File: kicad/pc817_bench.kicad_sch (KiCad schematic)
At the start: 15 parts, among them J1 24V + e-stops, U1 PC817, U2 PC817

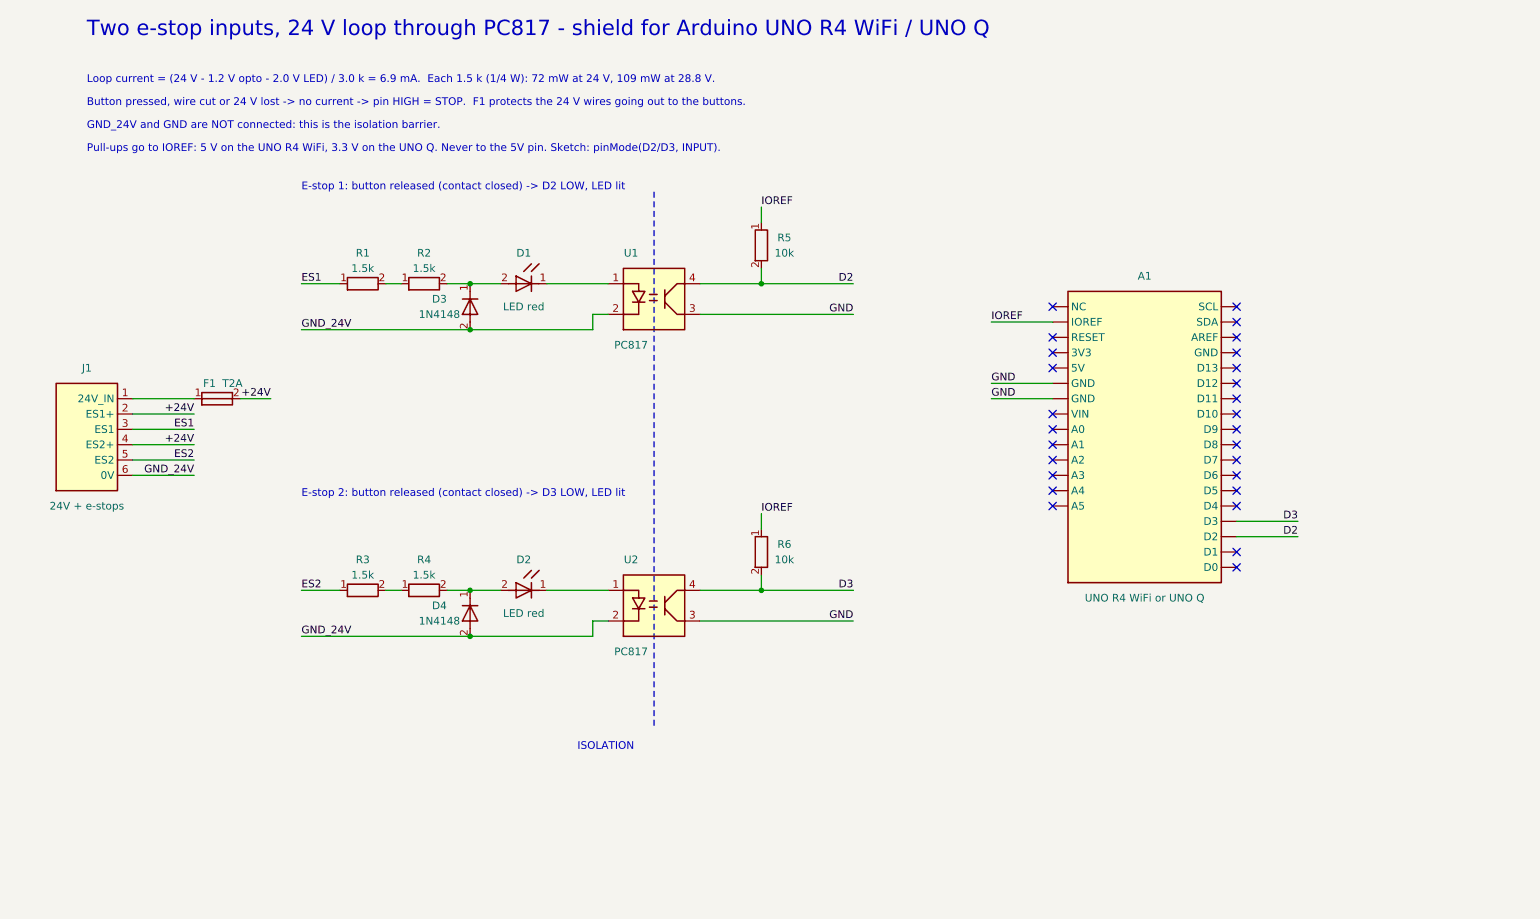
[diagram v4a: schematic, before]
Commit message: Four channels: two e-stop loops (D2, D3) and two lidar inputs (D4, D5)
9-way 3.5 mm terminal, fuse on the 24 V going out to the buttons, channels at
10 mm pitch. DRC: no errors, schematic parity OK (KiCad 10.0.6).

Co-Authored-By: Claude Fable 5.1 <noreply@anthropic.com>
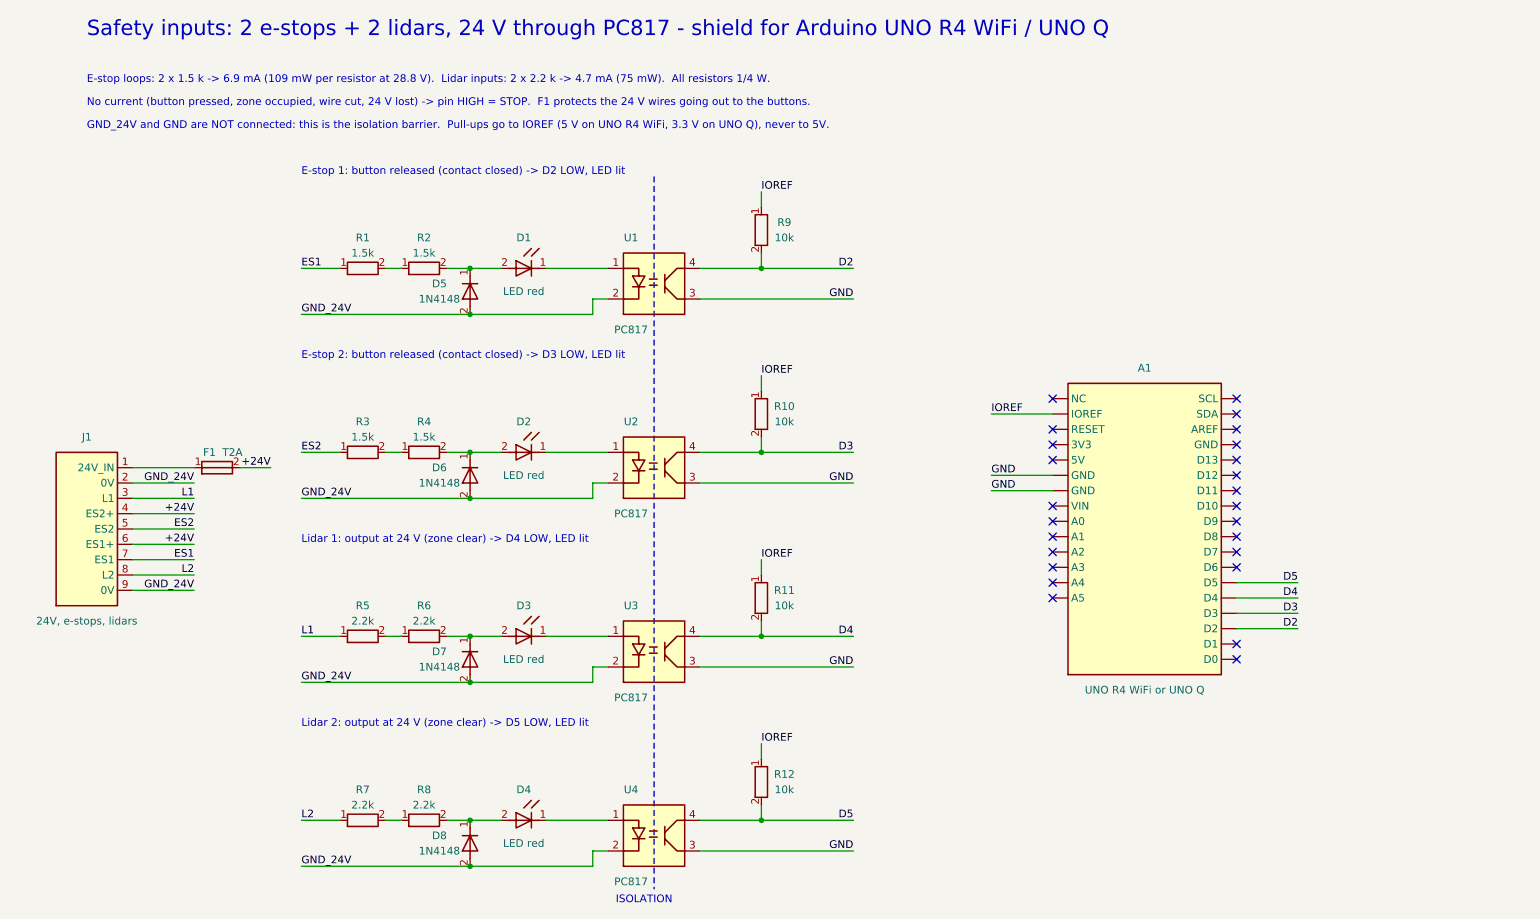
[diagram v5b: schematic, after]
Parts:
- removed J1: 24V + e-stops, TerminalBlock_Phoenix:TerminalBlock_Phoenix_MKDS-1,5-6_1x06_P5.00mm_Horizontal, symbol bench:CONN6
- added D4: LED red, LED_THT:LED_D3.0mm, symbol bench:LED_H
- added D7, D8: 1N4148, Diode_THT:D_DO-35_SOD27_P7.62mm_Horizontal, symbol bench:D_V
- added F1: T2A, Fuse:Fuse_Littelfuse_372_D8.50mm, symbol bench:FUSE_H
- added J1: 24V, e-stops, lidars, TerminalBlock_Phoenix:TerminalBlock_Phoenix_PT-1,5-9-3.5-H_1x09_P3.50mm_Horizontal, symbol bench:CONN9
- added R11, R12: 10k, Resistor_THT:R_Axial_DIN0207_L6.3mm_D2.5mm_P10.16mm_Horizontal, symbol bench:R_V
- added R5, R6, R7, R8: 2.2k, Resistor_THT:R_Axial_DIN0207_L6.3mm_D2.5mm_P10.16mm_Horizontal, symbol bench:R_H
- added U3, U4: PC817, Package_DIP:DIP-4_W7.62mm, symbol bench:PC817
- D3: renamed from F1; value T2A -> LED red; footprint Fuse:Fuse_Littelfuse_372_D8.50mm -> LED_THT:LED_D3.0mm; symbol bench:FUSE_H -> bench:LED_H
- renumbered D3 to D5, D4 to D6, R6 to R10, R5 to R9
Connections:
- net +24V: now also F1.2, J1.4 (ES2+), J1.6 (ES1+); no longer D3.2
- net ES1: now also J1.7 (ES1)
- net ES2: now also J1.5 (ES2)
- net GND: now also U3.3 (E), U4.3 (E)
- net GND_24V: now also D7.2 (A), D8.2 (A), J1.2 (0V), J1.9 (0V), U3.2 (K), U4.2 (K)
- net IOREF: now also R11.1, R12.1
- net at D3.1 (K): now also U3.1 (A)
- net D4: now reaches A1.19 (D4)
- net D4: now also R11.2, U3.4 (C)
- net D5: now reaches A1.20 (D5)
- net D5: now also R12.2, U4.4 (C)
- new net: D4.1 (K), U4.1 (A)
- new net: D3.2 (A), D7.1 (K), R6.2
- new net: R5.2, R6.1
- new net: R7.2, R8.1
- new net: D4.2 (A), D8.1 (K), R8.2
- new net: F1.1, J1.1 (24V_IN)
- new net L1: J1.3 (L1), R5.1
- new net L2: J1.8 (L2), R7.1
- no-connect marks 27 -> 25
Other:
- note added: "E-stop loops: 2 x 1.5 k -> 6.9 mA (109 mW per resistor at 28.8 V). Lidar inputs: 2 x 2.2 k -> 4.7 mA (75 mW). All resistors 1/4 W."
- note added: "GND_24V and GND are NOT connected: this is the isolation barrier. Pull-ups go to IOREF (5 V on UNO R4 WiFi, 3.3 V on UNO Q), never to 5V."
- note added: "Lidar 1: output at 24 V (zone clear) -> D4 LOW, LED lit"
- note added: "Lidar 2: output at 24 V (zone clear) -> D5 LOW, LED lit"
- note added: "No current (button pressed, zone occupied, wire cut, 24 V lost) -> pin HIGH = STOP. F1 protects the 24 V wires going out to the buttons."
- note added: "Safety inputs: 2 e-stops + 2 lidars, 24 V through PC817 - shield for Arduino UNO R4 WiFi / UNO Q"
- note removed: "Button pressed, wire cut or 24 V lost -> no current -> pin HIGH = STOP. F1 protects the 24 V wires going out to the buttons."
- note removed: "GND_24V and GND are NOT connected: this is the isolation barrier."
- note removed: "Loop current = (24 V - 1.2 V opto - 2.0 V LED) / 3.0 k = 6.9 mA. Each 1.5 k (1/4 W): 72 mW at 24 V, 109 mW at 28.8 V."
- note removed: "Pull-ups go to IOREF: 5 V on the UNO R4 WiFi, 3.3 V on the UNO Q. Never to the 5V pin. Sketch: pinMode(D2/D3, INPUT)."
- note removed: "Two e-stop inputs, 24 V loop through PC817 - shield for Arduino UNO R4 WiFi / UNO Q"
- title: E-stop inputs: 24 V loop through PC817 -> Safety inputs: 2 e-stops + 2 lidars
- moved on the sheet: D1, D2, D5, D6, R1, R10, R2, R3, R4, R9, U1, U2

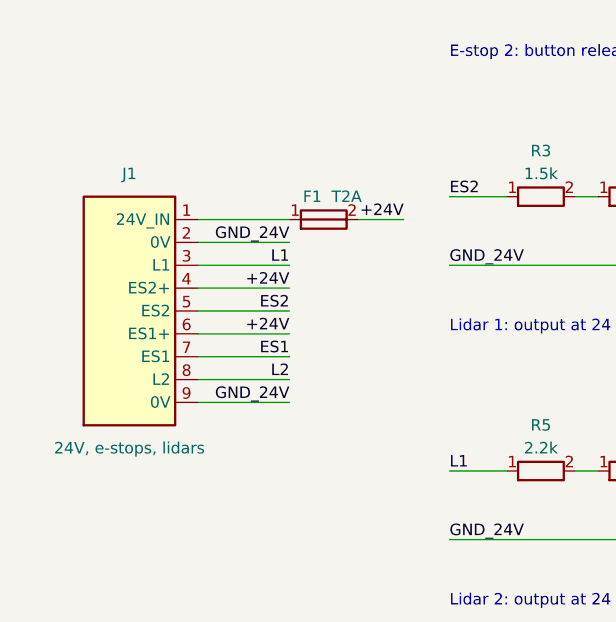
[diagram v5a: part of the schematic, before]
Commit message: Proto-shield variant in KiCad: grid footprints, 8-way terminal, board file models the build plan
Solder bridges and bare-wire runs are solder-side tracks; insulated wires stay
as ratsnest. check.sh verifies parity with the schematic and the wire count.
Plan reworked for physical clearances (diode away from the LED, fuse clear of
the header and terminal): 16 x 16 pads.

Co-Authored-By: Claude Fable 5.1 <noreply@anthropic.com>
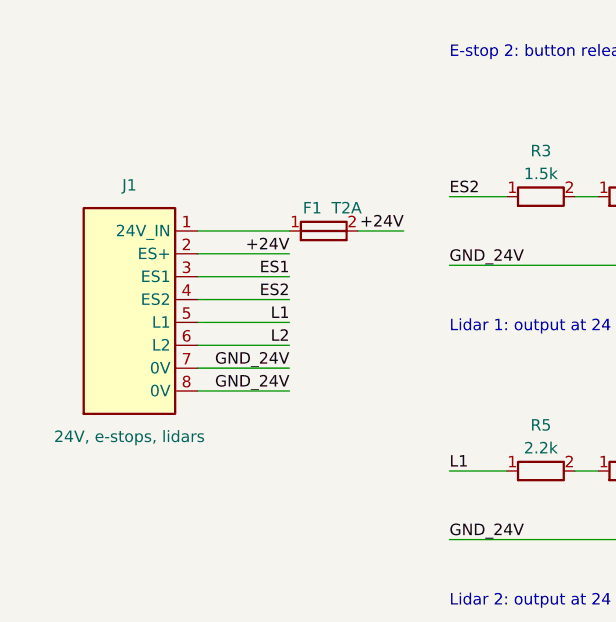
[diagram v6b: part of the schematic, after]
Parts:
- removed J1: 24V, e-stops, lidars, TerminalBlock_Phoenix:TerminalBlock_Phoenix_PT-1,5-9-3.5-H_1x09_P3.50mm_Horizontal, symbol bench:CONN9
- added J1: 24V, e-stops, lidars, TerminalBlock_Phoenix:TerminalBlock_Phoenix_MKDS-1,5-8-5.08_1x08_P5.08mm_Horizontal, symbol bench:CONN8
- D5, D6, D7, D8: footprint Diode_THT:D_DO-35_SOD27_P7.62mm_Horizontal -> Diode_THT:D_DO-35_SOD27_P2.54mm_Vertical_CathodeUp
- R1, R10, R11, R12, R2, R3, R4, R5, R6, R7, R8, R9: footprint Resistor_THT:R_Axial_DIN0207_L6.3mm_D2.5mm_P10.16mm_Horizontal -> Resistor_THT:R_Axial_DIN0207_L6.3mm_D2.5mm_P2.54mm_Vertical
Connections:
- net +24V: now also J1.2 (ES+)
- net ES1: now also J1.3 (ES1)
- net ES2: now also J1.4 (ES2)
- net GND_24V: now also J1.7 (0V), J1.8 (0V)
- net L1: now also J1.5 (L1)
- net L2: now also J1.6 (L2)
- net at F1.1: now also J1.1 (24V_IN)
